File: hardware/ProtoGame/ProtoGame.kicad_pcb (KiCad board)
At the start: 2 copper layers, 70 x 140.5 mm, 36 parts, among them J1 SD_Card_Module, SW1 SW_DPST_x2, SW10 SW_MEC_5E, SW2 SW_MEC_5E, SW3 SW_MEC_5E, SW4 SW_MEC_5E, SW5 SW_MEC_5E, SW6 SW_MEC_5E, SW7 SW_MEC_5E, SW8 SW_MEC_5E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

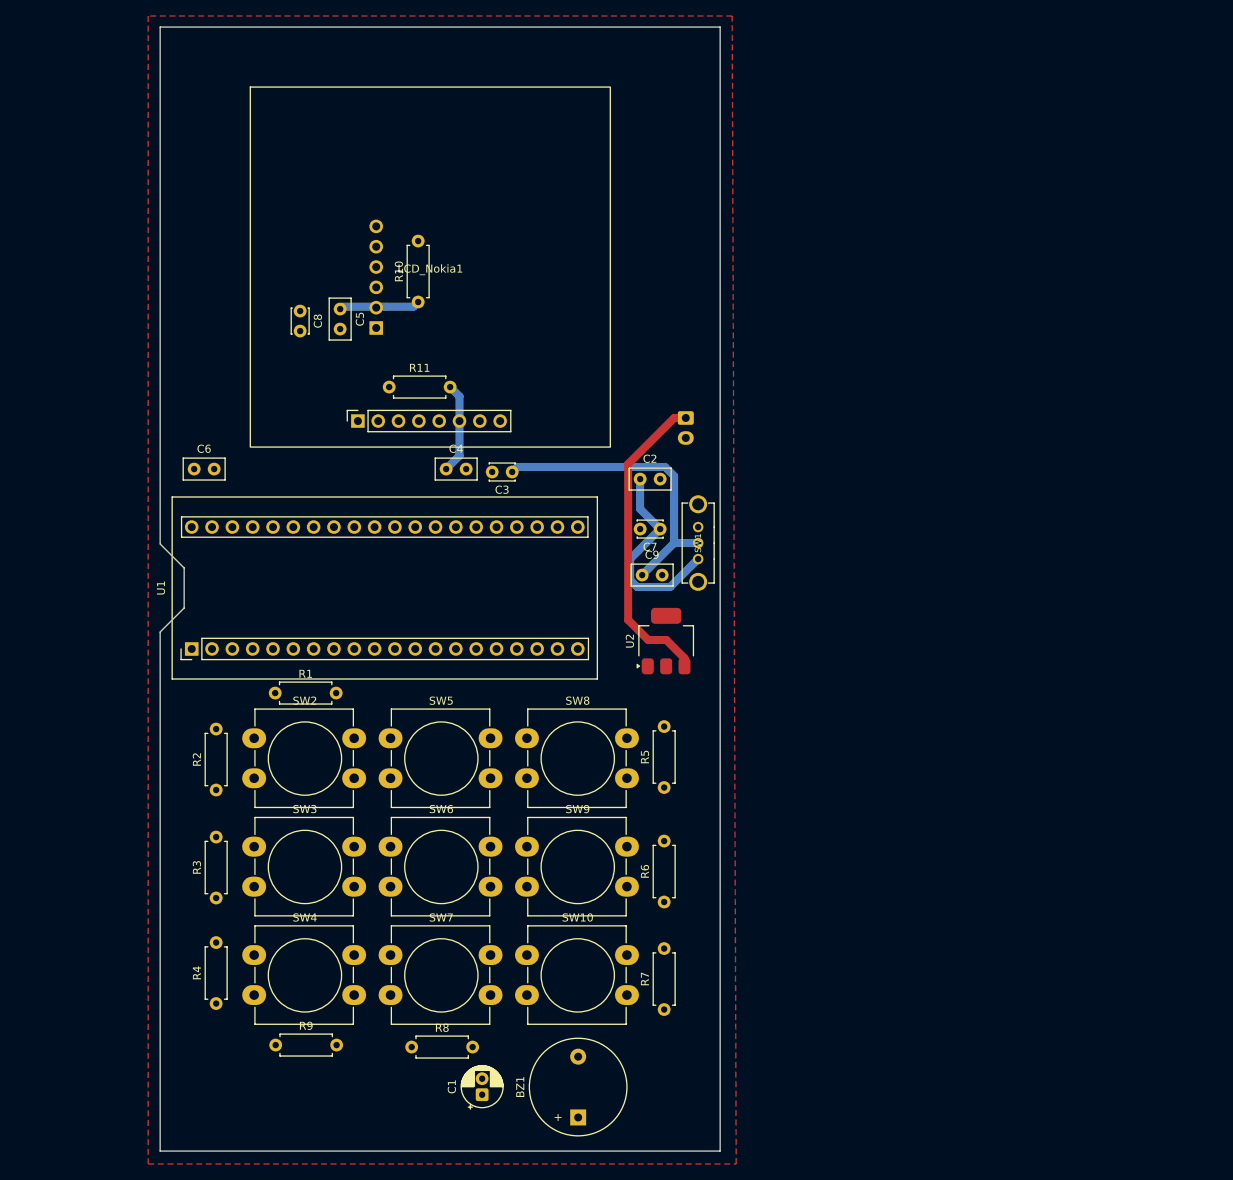
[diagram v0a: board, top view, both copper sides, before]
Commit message: ProtoGame v2 its complete and with new design, add assets images: footprint and 3d model
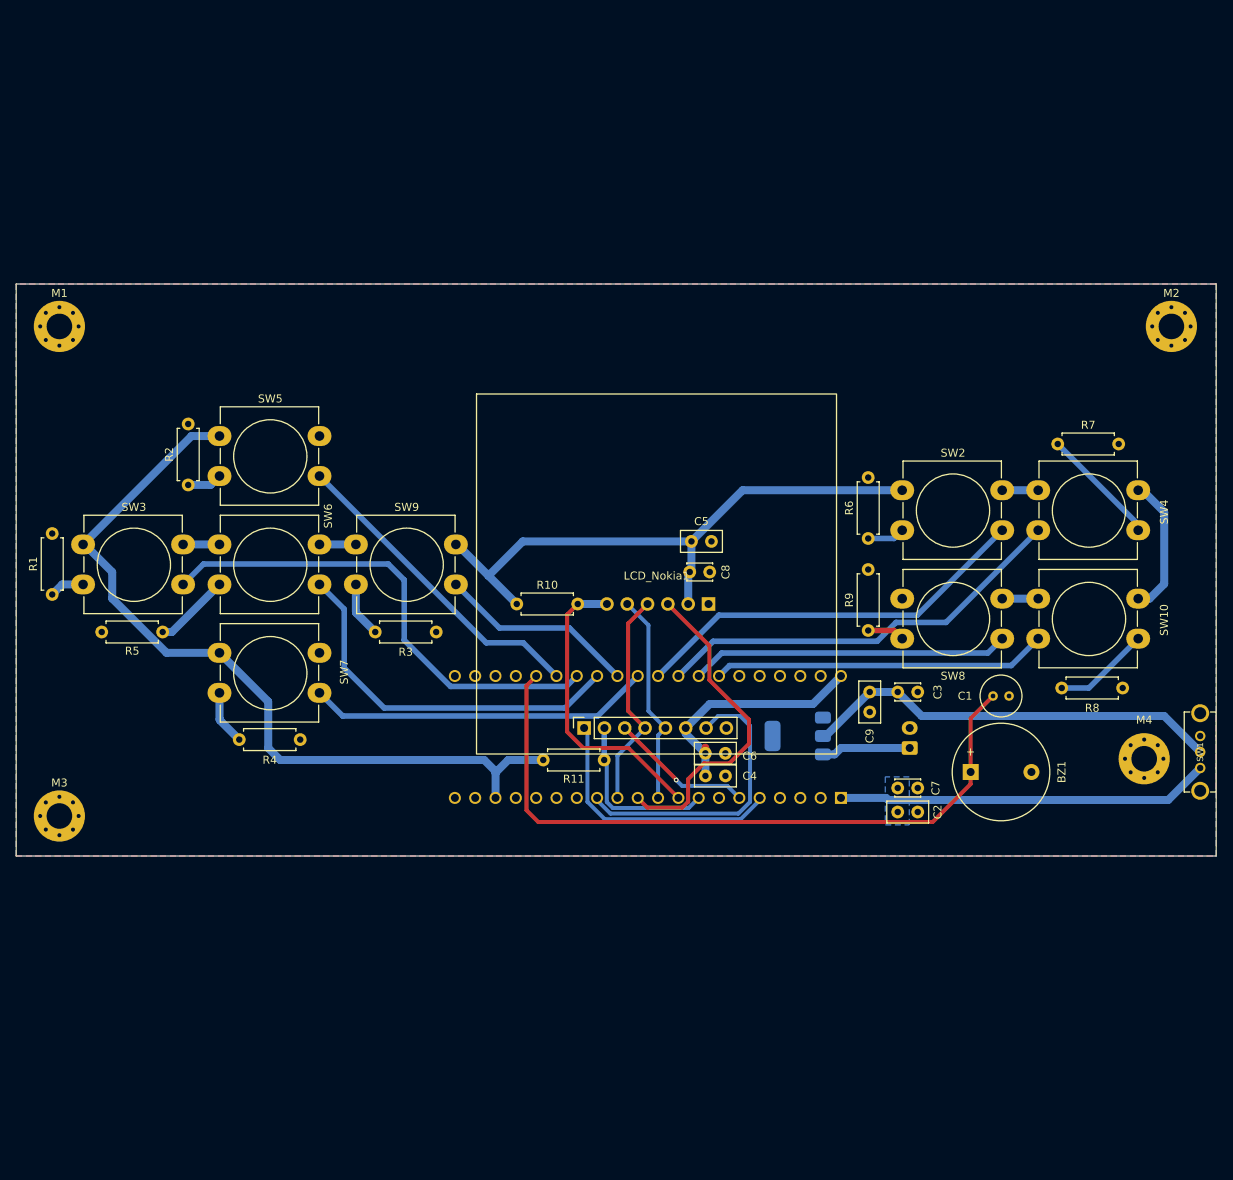
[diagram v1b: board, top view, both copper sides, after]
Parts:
- added M1: MountingHole_3.2mm_M3_Pad_Via, MountingHole:MountingHole_3.2mm_M3_Pad_Via, F.Cu at (76.9, 68.8)
- added M2: MountingHole_3.2mm_M3_Pad_Via, MountingHole:MountingHole_3.2mm_M3_Pad_Via, F.Cu at (215.9, 68.8)
- added M3: MountingHole_3.2mm_M3_Pad_Via, MountingHole:MountingHole_3.2mm_M3_Pad_Via, F.Cu at (76.9, 130.0)
- added M4: MountingHole_3.2mm_M3_Pad_Via, MountingHole:MountingHole_3.2mm_M3_Pad_Via, F.Cu at (212.5, 122.8)
- C1: footprint Capacitor_THT:CP_Radial_D5.0mm_P2.00mm -> Capacitor_THT:C_Radial_D5.0mm_H5.0mm_P2.00mm
- U1: footprint STM32:YAAJ_BluePill_2 -> STM32:MODULE_ZC323000-with-pinholder; moved to B.Cu
- U2: moved to B.Cu
- moved SW4 113.9 mm to (199.2, 89.3)
- moved R8 92.8 mm to (202.2, 114.0)
- moved R9 90.4 mm to (178.0, 106.8), turned to 90 degrees
- moved SW2 86.7 mm to (182.2, 89.3)
- moved R7 86.1 mm to (201.7, 83.5), turned to 0 degrees
- moved C1 81.0 mm to (193.6, 115.0), turned to 0 degrees
- moved SW10 77.9 mm to (199.2, 102.8)
- moved C6 73.1 mm to (157.6, 122.2)
- moved SW1 68.0 mm to (219.5, 122.0)
- moved R5 65.6 mm to (89.8, 107.0), turned to 180 degrees
- moved BZ1 65.4 mm to (190.8, 124.5), turned to 0 degrees
- moved C8 58.6 mm to (155.7, 99.5), turned to 0 degrees
- moved U1 58.1 mm to (150.5, 120.1)
- moved C3 55.5 mm to (181.7, 114.5), turned to 0 degrees
- moved J1 54.0 mm to (158.0, 103.5), turned to 90 degrees
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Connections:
- net Net-(BT1-+) renamed +3.7V
- C2 pad 1: +3.3V -> VCC
- C4 pad 1: Net-(LCD_Nokia1-VCC) -> +3.3V
- C4 pad 2: Net-(LCD_Nokia1-GND) -> GND
- C5 pad 1: Net-(J1-VCC) -> +3.3V
- C6 pad 1: unconnected-(C6-Pad1) -> +3.3V
- C6 pad 2: unconnected-(C6-Pad2) -> GND
- C7 pad 1: +3.3V -> VCC
- C8 pad 1: unconnected-(C8-Pad1) -> +3.3V
- C8 pad 2: unconnected-(C8-Pad2) -> GND
- J1 pad 2: Net-(J1-VCC) -> +3.3V
- LCD_Nokia1 pad 2: LCD_CE -> LCD_CS
- LCD_Nokia1 pad 6: Net-(LCD_Nokia1-VCC) -> +3.3V
- LCD_Nokia1 pad 8: Net-(LCD_Nokia1-GND) -> GND
- R1 pad 2: Net-(R1-Pad2) -> GND
- R10 pad 1: Net-(J1-VCC) -> +3.3V
- R11 pad 1: LCD_CE -> LCD_CS
- R11 pad 2: Net-(LCD_Nokia1-VCC) -> +3.3V
- R2 pad 2: Net-(R1-Pad2) -> GND
- R3 pad 2: Net-(R1-Pad2) -> GND
- R4 pad 2: Net-(R4-Pad2) -> GND
- R5 pad 2: Net-(R4-Pad2) -> GND
- R6 pad 2: Net-(R4-Pad2) -> GND
- R7 pad 2: Net-(R7-Pad2) -> GND
- R8 pad 2: Net-(R7-Pad2) -> GND
- R9 pad 2: Net-(R7-Pad2) -> GND
- SW1 pad 1: +3.3V -> VCC
- SW10 pad 1: Net-(SW10-Pad1) -> +3.3V
- SW10 pad 2: unconnected-(SW10-Pad2)_1 -> Net-(SW3-K)
- SW2 pad 1: Net-(SW2-Pad1) -> +3.3V
- SW2 pad 2: unconnected-(SW2-Pad2) -> B6
- SW3 pad 1: Net-(SW2-Pad1) -> +3.3V
- SW3 pad 2: unconnected-(SW3-Pad2) -> B2
- SW4 pad 1: Net-(SW2-Pad1) -> +3.3V
- SW4 pad 2: unconnected-(SW4-Pad2)_1 -> Net-(SW2-K)
- SW5 pad 1: Net-(SW5-Pad1) -> +3.3V
- SW5 pad 2: unconnected-(SW5-Pad2)_1 -> B1
- SW6 pad 1: Net-(SW5-Pad1) -> +3.3V
- SW6 pad 2: unconnected-(SW6-Pad2)_1 -> B3
- SW7 pad 1: Net-(SW5-Pad1) -> +3.3V
- SW7 pad 2: unconnected-(SW7-Pad2) -> B5
- SW8 pad 1: Net-(SW10-Pad1) -> +3.3V
- SW8 pad 2: unconnected-(SW8-Pad2) -> B8
- SW9 pad 1: Net-(SW10-Pad1) -> +3.3V
- SW9 pad 2: unconnected-(SW9-Pad2) -> B4
- U1 pad 1: +3.3V -> VCC
- U1 pad 10: LCD_RST -> SCK
- U1 pad 11: LCD_DC -> MISO
- U1 pad 12: unconnected-(U1-PA2-Pad12) -> MOSI
- U1 pad 13: LCD_CS -> LCD_BL
- U1 pad 14: SD_CS -> unconnected-(U1-B1-Pad14)
- U1 pad 15: SCK -> unconnected-(U1-B10-Pad15)
- U1 pad 16: MISO -> unconnected-(U1-B11-Pad16)
- U1 pad 17: MOSI -> unconnected-(U1-R-Pad17)
- U1 pad 18: LCD_BL -> +3.3V
- U1 pad 19: unconnected-(U1-PB1-Pad19) -> GND
- U1 pad 20: unconnected-(U1-PB2-Pad20) -> GND
- U1 pad 23: GND -> unconnected-(U1-B14-Pad23)
- U1 pad 24: +3.3V -> unconnected-(U1-B15-Pad24)
- U1 pad 25: unconnected-(U1-PB12-Pad25) -> Buz
- U1 pad 26: unconnected-(U1-PB13-Pad26) -> B1
- U1 pad 27: unconnected-(U1-PB14-Pad27) -> B2
- U1 pad 28: unconnected-(U1-PB15-Pad28) -> B3
- U1 pad 29: BUZ -> B4
- U1 pad 30: B1 -> B5
- U1 pad 31: B2 -> B6
- U1 pad 32: B3 -> B7
- U1 pad 33: B4 -> B8
- U1 pad 34: unconnected-(U1-PA13-Pad34) -> B9
- U1 pad 35: GND -> unconnected-(U1-B7-Pad35)
- U1 pad 36: +3.3V -> unconnected-(U1-B8-Pad36)
- U1 pad 38: B5 -> unconnected-(U1-5V-Pad38)
- U1 pad 39: B6 -> GND
- U1 pad 40: B7 -> +3.3V
- U1 pad 5: unconnected-(U1-PD0-Pad5) -> LCD_RST
- U1 pad 6: unconnected-(U1-PD1-Pad6) -> LCD_DC
- U1 pad 8: GND -> LCD_CS
- U1 pad 9: +3.3V -> SD_CS
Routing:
- net +3.3V: track 25.5 -> 241.9 mm
- net Buz: track 0.00 -> 87.5 mm
- net B2: track 0.00 -> 61.6 mm
- net B7: track 0.00 -> 52.5 mm
- net B6: track 0.00 -> 50.6 mm
- net B3: track 0.00 -> 47.1 mm
- net VCC: track 0.00 -> 46.7 mm
- net B5: track 0.00 -> 43.1 mm
- net B9: track 0.00 -> 41.8 mm
- net MISO: track 0.00 -> 41.0 mm
- net B1: track 0.00 -> 40.0 mm
- net B8: track 0.00 -> 39.9 mm
- net SD_CS: track 0.00 -> 37.5 mm
- net LCD_BL: track 0.00 -> 36.8 mm
- net LCD_RST: track 0.00 -> 33.1 mm
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- added copper zone on B.Cu, net GND
- added copper zone on B.Cu, net VCC
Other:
- board size 70 x 140.5 mm -> 150 x 71.5 mm

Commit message: add 'frufrus' in pcb
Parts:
- added REF**: OSHW-Logo_11.4x12mm_Copper, Symbol:OSHW-Logo_11.4x12mm_Copper, F.Cu at (89.0, 126.0)
- added REF**: Symbol_ESD-Logo_CopperTop, Symbol:Symbol_ESD-Logo_CopperTop, F.Cu at (82.0, 84.0)
- added REF**: KiCad-Logo2_12mm_Copper, Symbol:KiCad-Logo2_12mm_Copper, F.Cu at (194.0, 71.5)
